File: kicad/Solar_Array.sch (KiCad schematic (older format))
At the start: 17 parts, among them IC1 SPV1040, P1 PV_CELL, Q1 Q_NPN_BCE, U1 LTC2990

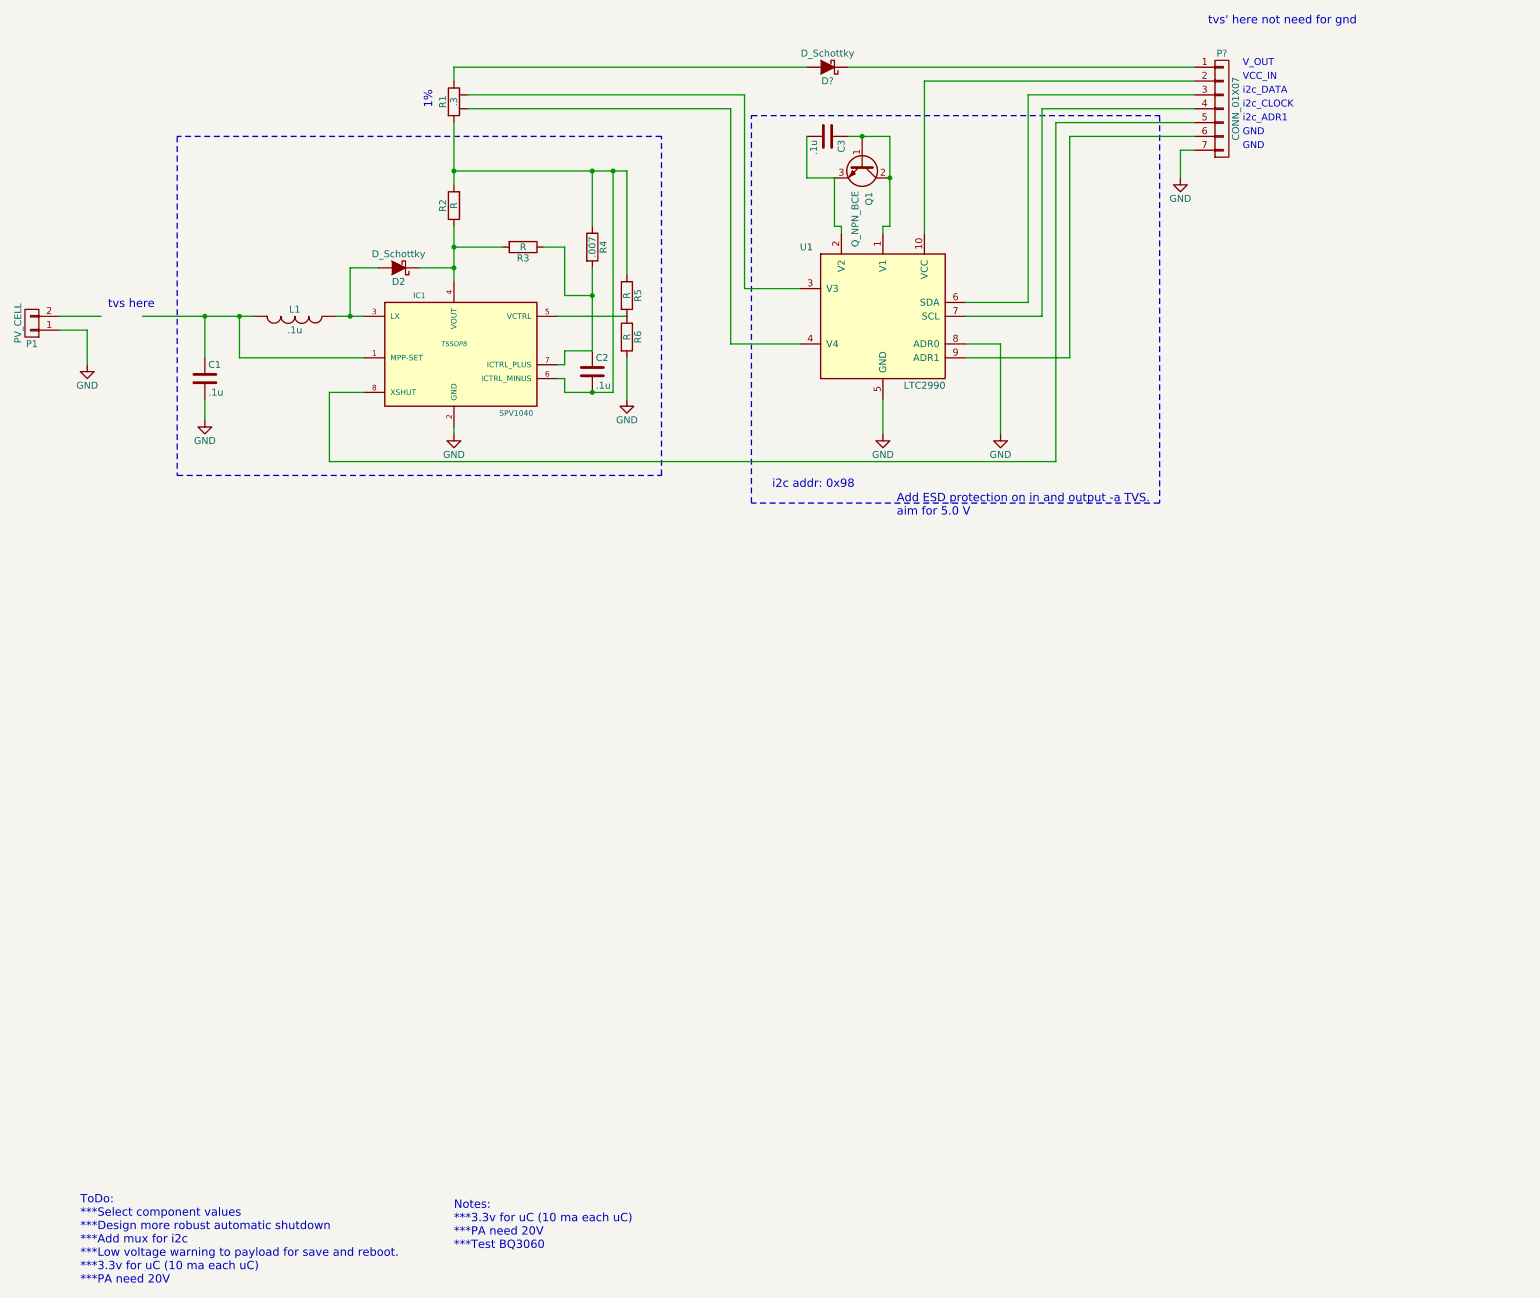
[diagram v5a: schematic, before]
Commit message: Fixed voltage divider from SPV1040, Added Vctrl Divider component values, added Shunt to Vout of 1040, added TVS to PV in and to output bus.
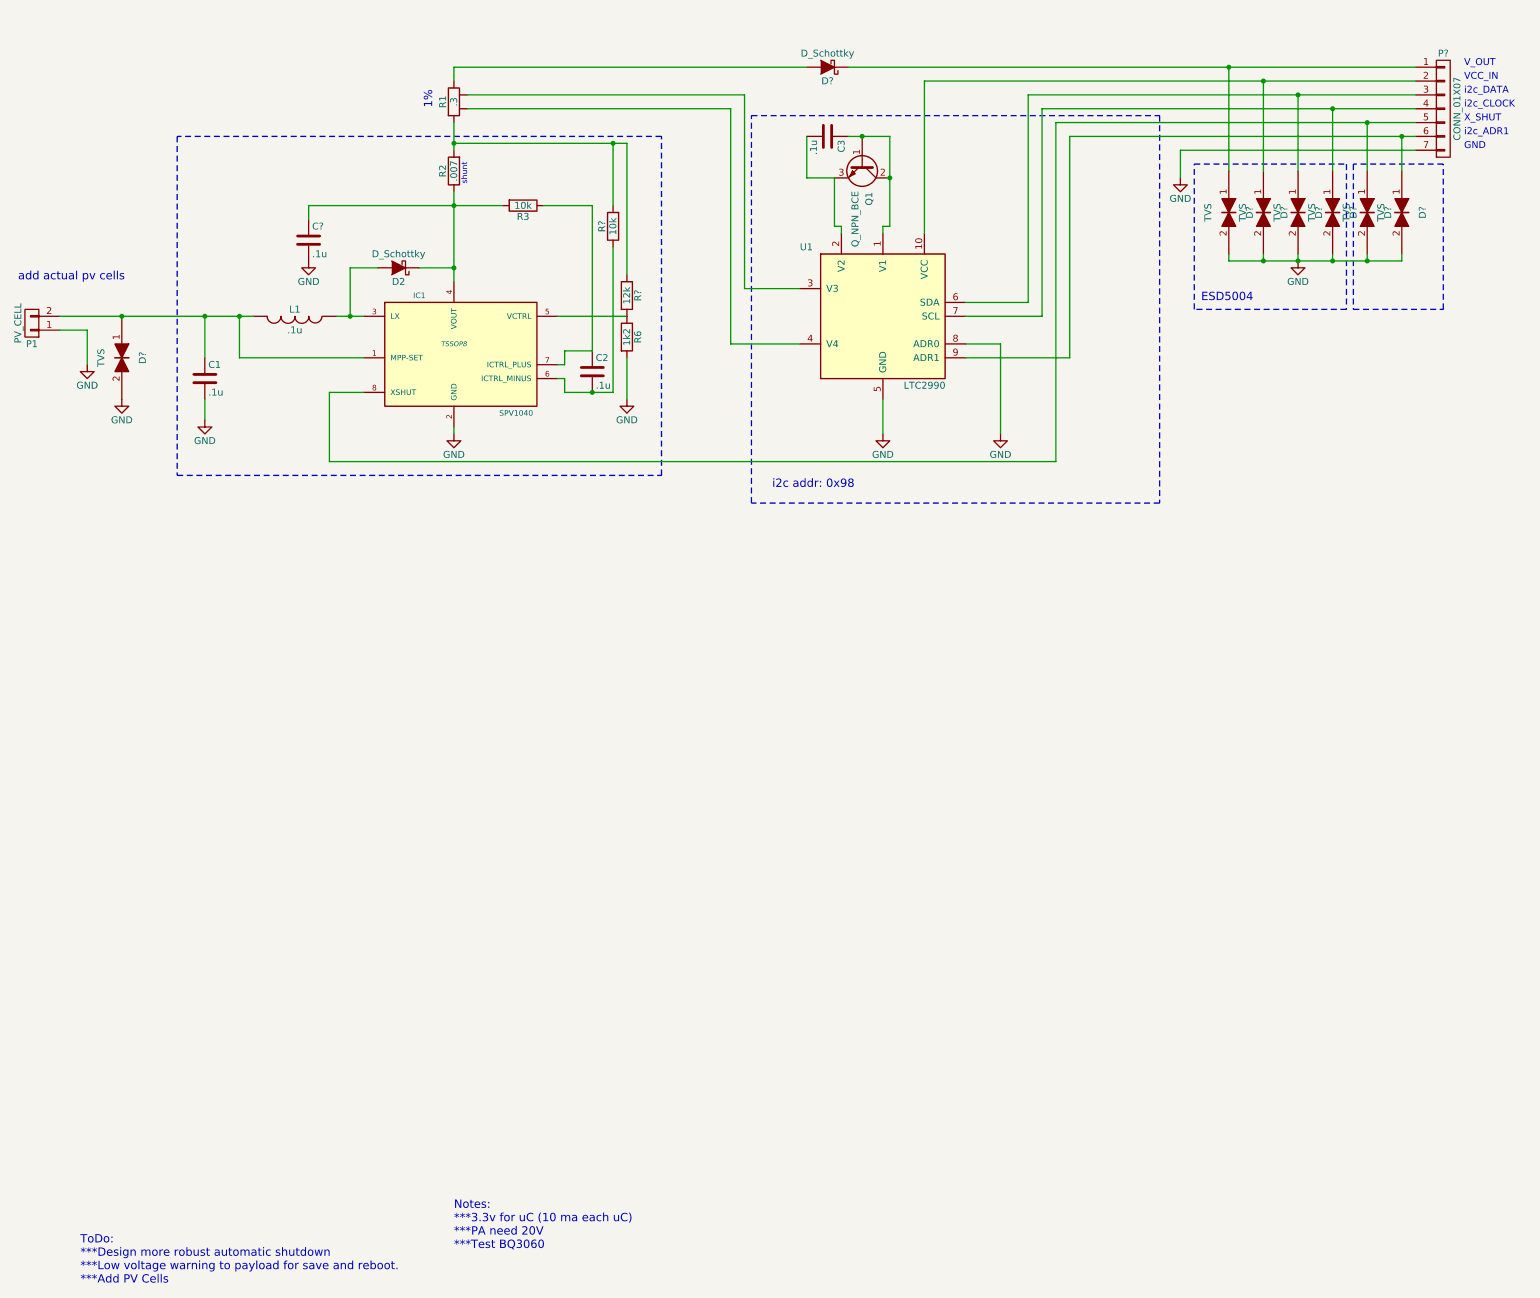
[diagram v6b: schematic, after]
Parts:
- removed R4: .007, symbol R
- added C?: .1u, symbol C
- added D? (x7): TVS, symbol TVS
- added R?: 10k, symbol R
- R2: value R -> .007
- R3: value R -> 10k
- R6: value R -> 1k2
- R?: renamed from R5; value R -> 12k
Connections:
- net GND: now also C?.2, D?.2, D?.2, D?.2, D?.2, D?.2, D?.2, D?.2
- net at P?.2 (P2), U1.10 (VCC): now also D?.1
- net at P?.3 (P3), U1.6 (SDA): now also D?.1
- net at P?.4 (P4), U1.7 (SCL): now also D?.1
- net at P?.6 (P6), U1.9 (ADR1): now also D?.1
- net at R1.2, R2.2, R?.1: now also R?.2; no longer C2.2, IC1.6 (ICTRL_MINUS)
- net at C1.1, IC1.1 (MPP-SET), L1.2: now also P1.2 (P2), D?.1
- net at D2.1 (K), IC1.4 (VOUT), R2.1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: now also C?.1
- net at IC1.8 (XSHUT), P?.5 (P5): now also D?.1
- net at D?.1 (K), P?.1 (P1): now also D?.1
- new net: C2.2, IC1.6 (ICTRL_MINUS), R?.1
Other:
- note added: "ESD5004"
- note added: "ToDo:\n***Design more robust automatic shutdown\n***Low voltage warning to payload for save and reboot.\n***Add PV Cells"
- note added: "X_SHUT"
- note added: "add actual pv cells"
- note added: "shunt"
- note removed: "Add ESD protection on in and output -a TVS.\naim for 5.0 V"
- note removed: "ToDo:\n***Select component values\n***Design more robust automatic shutdown\n***Add mux for i2c\n***Low voltage warning to payload for save and reboot.\n***3.3v for uC (10 ma each uC)\n***PA need 20V"
- note removed: "tvs here"
- note removed: "tvs' here not need for gnd"
- moved on the sheet: P?, R2, R3
